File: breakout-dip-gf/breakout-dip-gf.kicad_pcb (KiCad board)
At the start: 4 copper layers, 19 x 42.1 mm, 61 parts, among them J1 USB_C, SW1 434121025816, U1 TT_GF_COB, U2 CH32X035G8U6, U3 AP2112K-3.3

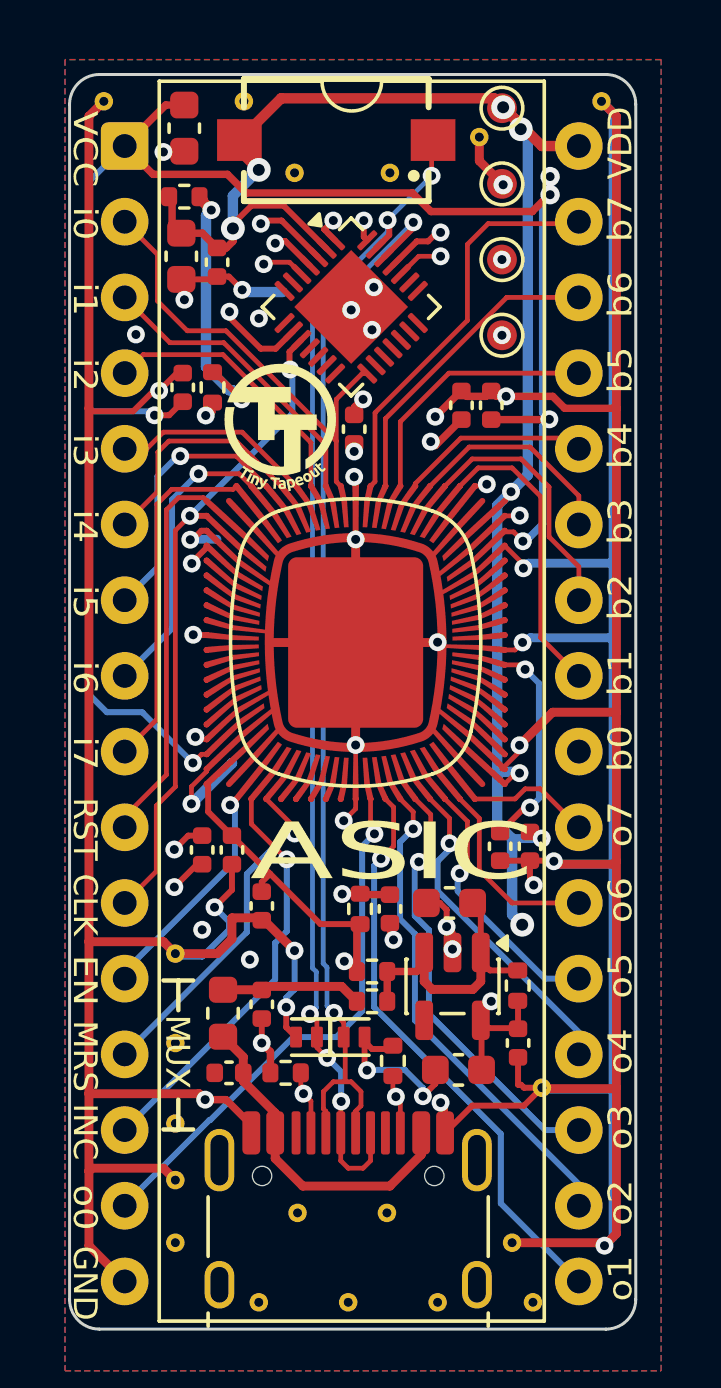
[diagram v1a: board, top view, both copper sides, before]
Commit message: remap/reroute of pclk and VAA to Vcore
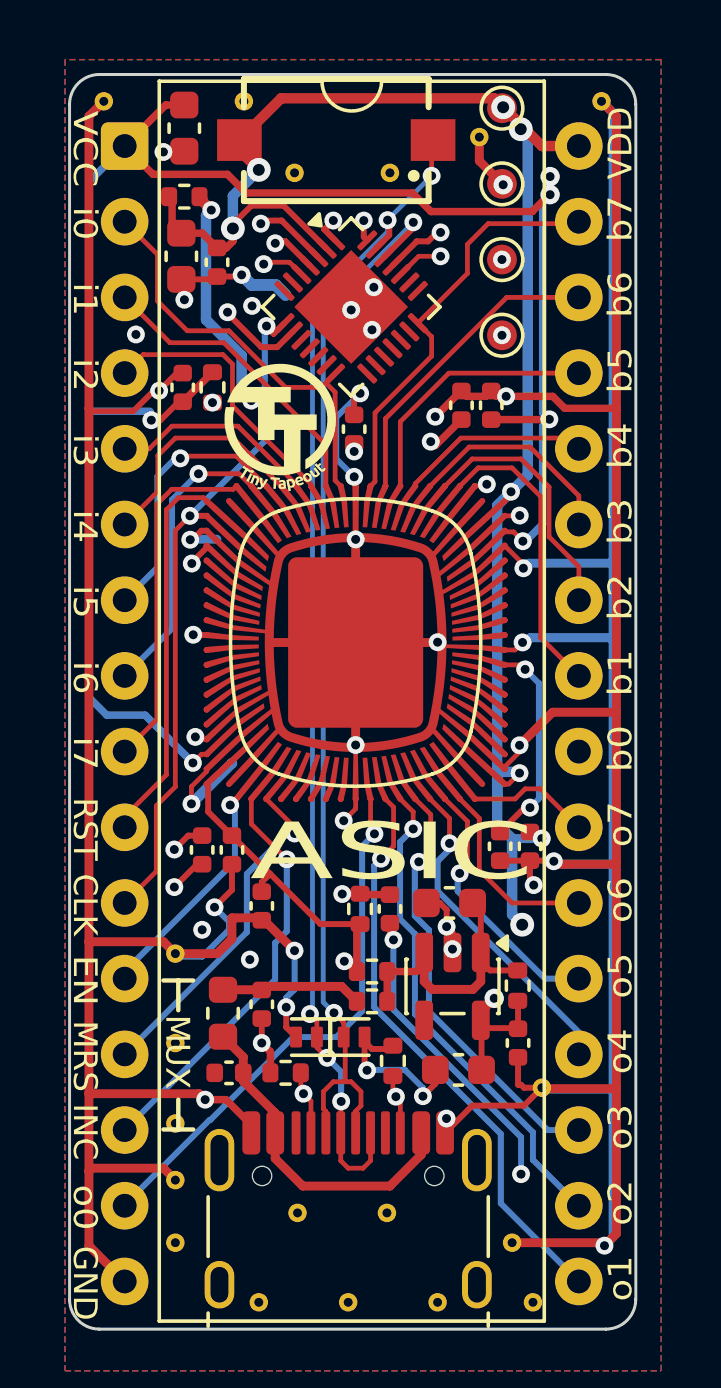
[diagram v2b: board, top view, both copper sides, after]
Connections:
- R6 pad 1: VIO_{REG} -> VDD_{CORE}
- U2 pad 10: /p_clk -> unconnected-(U2-PA5-Pad10)
- U2 pad 14: unconnected-(U2-PB3-Pad14) -> /uin0
- U2 pad 15: /uin0 -> unconnected-(U2-PB4-Pad15)
- U2 pad 21: unconnected-(U2-PB10-Pad21) -> /uio7
- U2 pad 8: unconnected-(U2-PA3-Pad8) -> /p_clk
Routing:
- net GND: track 573.9 -> 602.5 mm, vias 38 -> 39
- net VDD_{CORE}: track 74.7 -> 76.5 mm
- net /uin0: track 15.4 -> 14.1 mm
- net /p_clk: track 22.0 -> 22.9 mm
- net /CC1: track 34.4 -> 35.3 mm

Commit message: bonding house + gnd rework
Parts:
- added STITCH2: StitchingVia-0.3mm, flyingcarsfootprints:StitchingVia-0.3mm, F.Cu at (32.5, 61.2)
- moved STITCH2 0.40 mm to (34.3, 62.8)
- moved STITCH2 0.32 mm to (37.2, 61.7)
- moved SW1 0.30 mm to (32.4, 61.7)
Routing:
- net GND: track 602.5 -> 699.7 mm, vias 39 -> 40

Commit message: bonding fids, silk markings, v1.0
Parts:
- moved C18 0.10 mm to (29.6, 87.5)
- renumbered C3 to CONN1
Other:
- board text added: "1"
- board text added: "BOOT"
- board text added: "CK"
- board text added: "IO"
- board text added: "PRG"
- board text added: "VCR"
- board text removed: "VCC"

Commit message: CoB DIP, as panelized
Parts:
- added J2: 1x16P TH Pin Header, TinyTapeout:PinHeader_1x16_P2.54mm_Placeholder, B.Cu at (25.0, 61.9)
- added J3: 1x16P TH Pin Header, TinyTapeout:PinHeader_1x16_P2.54mm_Placeholder, B.Cu at (40.2, 61.9)

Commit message: docs and prettyfication
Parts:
- J2, J3: value 1x16P TH Pin Header -> PZ254-1-16-Z-8.5
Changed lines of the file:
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@@
 		(capping no)
 		(filling no)
+		(zone_defaults)
 		(aux_axis_origin 25 100)
 		(grid_origin 25 100)
@@
 			)
 		)
-		(property "Value" "1x16P TH Pin Header"
+		(property "Value" "PZ254-1-16-Z-8.5"
 			(at -0.025 -18.975 90)
 			(layer "B.Fab")
@@
 			)
 		)
-		(property "Value" "1x16P TH Pin Header"
+		(property "Value" "PZ254-1-16-Z-8.5"
 			(at 0 -18.9 270)
 			(layer "B.Fab")
